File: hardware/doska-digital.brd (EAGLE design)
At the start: 100.6 x 40.6 mm, 97 parts, among them Q1 12MHz

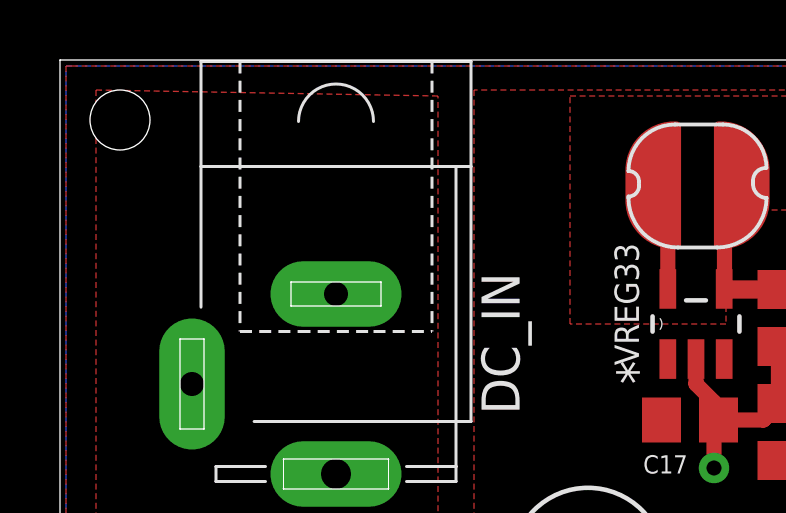
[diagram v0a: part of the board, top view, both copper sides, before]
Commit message: Fixed short of internal layers on digital board (eagle bug).
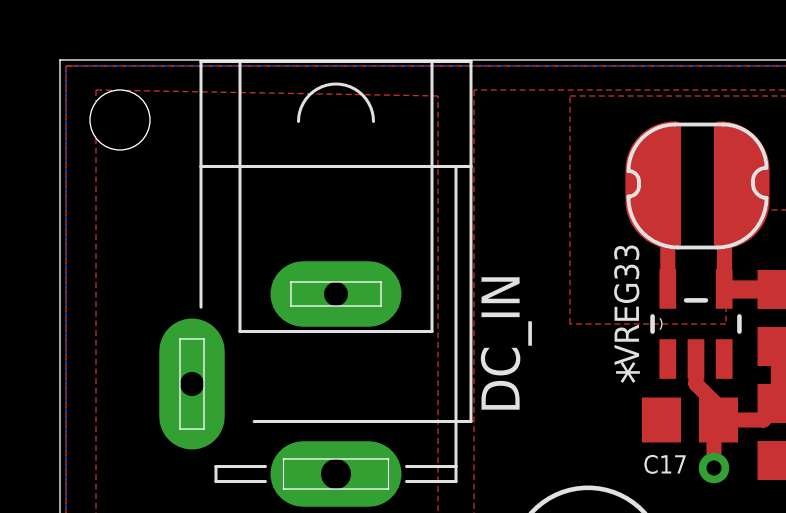
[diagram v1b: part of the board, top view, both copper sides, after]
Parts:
- DC_IN: device con-jack:SPC4078 -> doska-digital:CON-JACK_SPC4078
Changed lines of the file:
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@@
 <?xml version="1.0" encoding="utf-8"?>
 <!DOCTYPE eagle SYSTEM "eagle.dtd">
-<eagle version="6.3">
+<eagle version="6.2">
 <drawing>
 <settings>
@@
 <layers>
 <layer number="1" name="Top" color="4" fill="1" visible="yes" active="yes"/>
-<layer number="2" name="Route2" color="11" fill="1" visible="no" active="yes"/>
+<layer number="2" name="Route2" color="11" fill="1" visible="yes" active="yes"/>
 <layer number="3" name="Route3" color="4" fill="3" visible="no" active="no"/>
 <layer number="4" name="Route4" color="1" fill="4" visible="no" active="no"/>
@@
 <layer number="13" name="Route13" color="4" fill="5" visible="no" active="no"/>
 <layer number="14" name="Route14" color="1" fill="6" visible="no" active="no"/>
-<layer number="15" name="Route15" color="5" fill="1" visible="no" active="yes"/>
+<layer number="15" name="Route15" color="5" fill="1" visible="yes" active="yes"/>
 <layer number="16" name="Bottom" color="1" fill="1" visible="yes" active="yes"/>
 <layer number="17" name="Pads" color="2" fill="1" visible="yes" active="yes"/>
@@
 </class>
 </classes>
-<designrules name="default *">
+<designrules>
 <description language="de">&lt;b&gt;EAGLE Design Rules&lt;/b&gt;
 &lt;p&gt;
@@
 <attribute name="VALUE" x="62.686" y="12.562" size="1.27" layer="28" rot="MR270"/>
 </element>
-<element name="DC_IN" library="con-jack" package="SPC4078" value="" x="9.2" y="29.8" smashed="yes" rot="R270">
+<element name="DC_IN" library="doska-digital" package="CON-JACK_SPC4078" value="" x="9.2" y="29.8" smashed="yes" rot="R270">
 <attribute name="OC_NEWARK" value="unknown" x="9.2" y="29.8" size="1.778" layer="27" rot="R270" display="off"/>
 <attribute name="MPN" value="" x="9.2" y="29.8" size="1.778" layer="27" rot="R270" display="off"/>
@@
 <wire x1="49.4" y1="18.65" x2="43.45" y2="18.65" width="0.3048" layer="1"/>
 <wire x1="43.45" y1="18.65" x2="43.4" y2="18.6" width="0.3048" layer="1"/>
+<wire x1="4.4" y1="29.8" x2="9.2" y2="32.8" width="0" layer="19" extent="1-1"/>
+<wire x1="16.584" y1="23.8" x2="9.2" y2="32.8" width="0" layer="19" extent="1-1"/>
 </signal>
 <signal name="5V">
@@
 </polygon>
 <contactref element="DC_IN" pad="3"/>
+<wire x1="23.4" y1="2.46" x2="9.2" y2="26.8" width="0" layer="19" extent="1-1"/>
 </signal>
 <signal name="N$19">
